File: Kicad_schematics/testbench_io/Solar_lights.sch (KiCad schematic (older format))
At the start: 9 parts

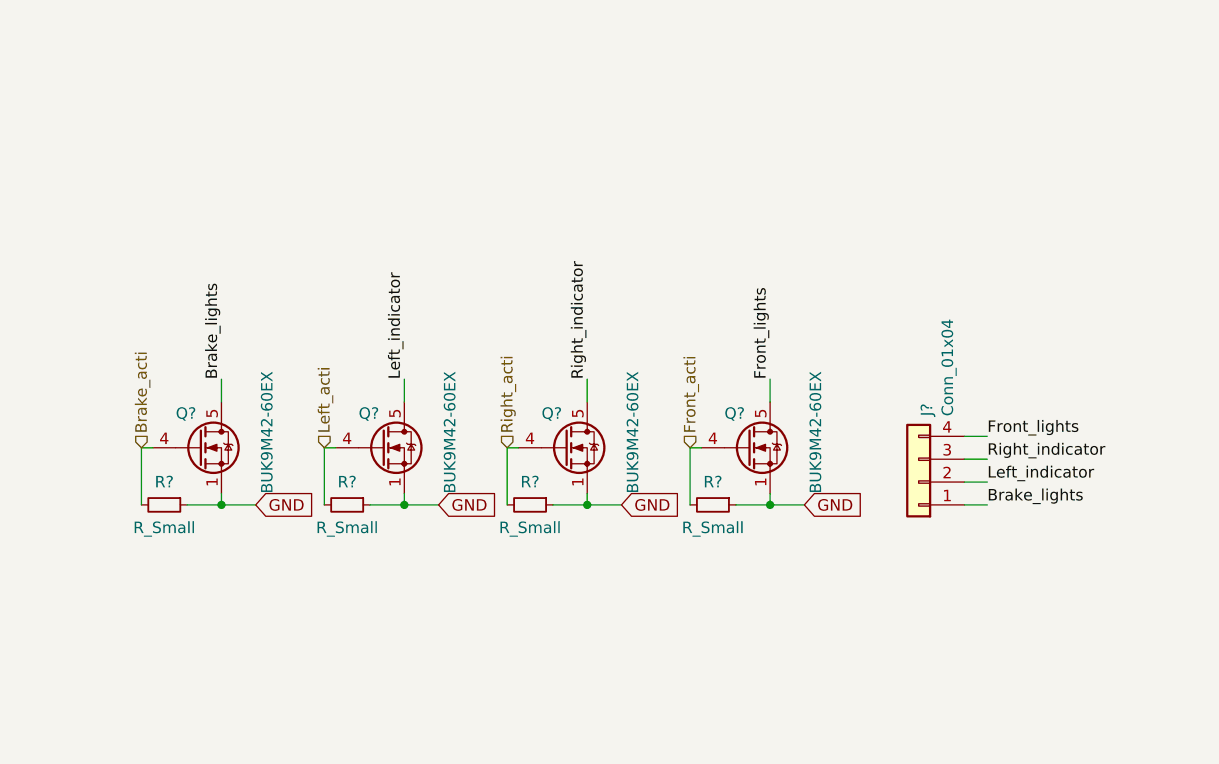
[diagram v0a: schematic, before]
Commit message: Added footprints
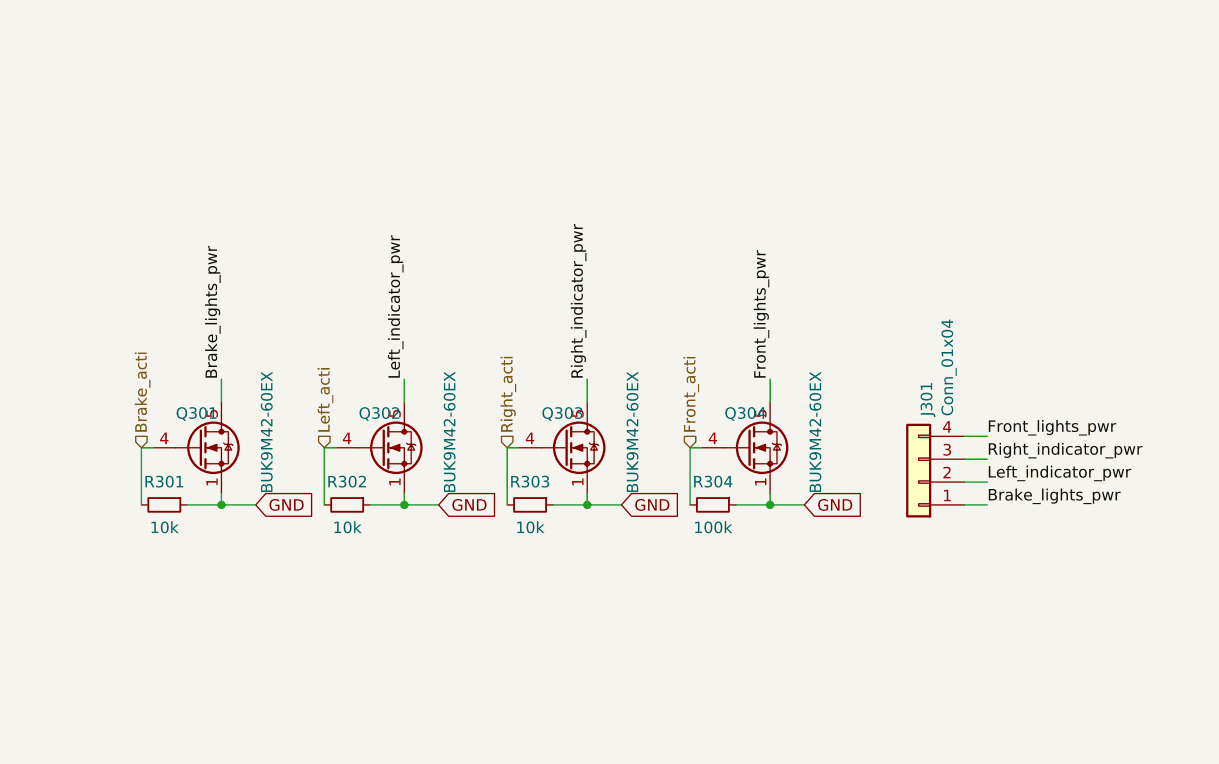
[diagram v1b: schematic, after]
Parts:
- R301, R302, R303: renamed from R?; value R_Small -> 10k
- R304: renamed from R?; value R_Small -> 100k
- gave numbers to parts that had none: 5
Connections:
- net Brake_lights renamed Brake_lights_pwr
- net Front_lights renamed Front_lights_pwr
- net Left_indicator renamed Left_indicator_pwr
- net Right_indicator renamed Right_indicator_pwr
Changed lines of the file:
@@
 	6750 3850 6750 3750
 Text Label 6750 3750 1    50   ~ 0
-Front_lights
+Front_lights_pwr
 Text GLabel 6900 4300 2    50   Input ~ 0
 GND
@@
 P 6500 4300
 AR Path="/60041E0C" Ref="R?"  Part="1"
-AR Path="/6001478F/60041E0C" Ref="R?"  Part="1"
-F 0 "R?" V 6400 4300 50  0000 C CNN
-F 1 "R_Small" V 6600 4300 50  0000 C CNN
+AR Path="/6001478F/60041E0C" Ref="R304"  Part="1"
+F 0 "R304" V 6400 4300 50  0000 C CNN
+F 1 "100k" V 6600 4300 50  0000 C CNN
 F 2 "" H 6500 4300 50  0001 C CNN
 F 3 "~" H 6500 4300 50  0001 C CNN
@@
 P 6650 4050
 AR Path="/60041E12" Ref="Q?"  Part="1"
-AR Path="/6001478F/60041E12" Ref="Q?"  Part="1"
-F 0 "Q?" H 6550 4200 50  0000 L CNN
+AR Path="/6001478F/60041E12" Ref="Q304"  Part="1"
+F 0 "Q304" H 6550 4200 50  0000 L CNN
 F 1 "BUK9M42-60EX" V 6950 3850 50  0000 L CNN
 F 2 "Package_TO_SOT_SMD:LFPAK33" H 6850 3975 50  0001 L CIN
@@
 	5950 3850 5950 3750
 Text Label 5950 3750 1    50   ~ 0
-Right_indicator
+Right_indicator_pwr
 Text GLabel 6100 4300 2    50   Input ~ 0
 GND
@@
 P 5700 4300
 AR Path="/60041E22" Ref="R?"  Part="1"
-AR Path="/6001478F/60041E22" Ref="R?"  Part="1"
-F 0 "R?" V 5600 4300 50  0000 C CNN
-F 1 "R_Small" V 5800 4300 50  0000 C CNN
+AR Path="/6001478F/60041E22" Ref="R303"  Part="1"
+F 0 "R303" V 5600 4300 50  0000 C CNN
+F 1 "10k" V 5800 4300 50  0000 C CNN
 F 2 "" H 5700 4300 50  0001 C CNN
 F 3 "~" H 5700 4300 50  0001 C CNN
@@
 P 5850 4050
 AR Path="/60041E28" Ref="Q?"  Part="1"
-AR Path="/6001478F/60041E28" Ref="Q?"  Part="1"
-F 0 "Q?" H 5750 4200 50  0000 L CNN
+AR Path="/6001478F/60041E28" Ref="Q303"  Part="1"
+F 0 "Q303" H 5750 4200 50  0000 L CNN
 F 1 "BUK9M42-60EX" V 6150 3850 50  0000 L CNN
 F 2 "Package_TO_SOT_SMD:LFPAK33" H 6050 3975 50  0001 L CIN
@@
 	5150 3850 5150 3750
 Text Label 5150 3750 1    50   ~ 0
-Left_indicator
+Left_indicator_pwr
 Text GLabel 5300 4300 2    50   Input ~ 0
 GND
@@
 P 4900 4300
 AR Path="/60041E38" Ref="R?"  Part="1"
-AR Path="/6001478F/60041E38" Ref="R?"  Part="1"
-F 0 "R?" V 4800 4300 50  0000 C CNN
-F 1 "R_Small" V 5000 4300 50  0000 C CNN
+AR Path="/6001478F/60041E38" Ref="R302"  Part="1"
+F 0 "R302" V 4800 4300 50  0000 C CNN
+F 1 "10k" V 5000 4300 50  0000 C CNN
 F 2 "" H 4900 4300 50  0001 C CNN
 F 3 "~" H 4900 4300 50  0001 C CNN
@@
 P 5050 4050
 AR Path="/60041E3E" Ref="Q?"  Part="1"
-AR Path="/6001478F/60041E3E" Ref="Q?"  Part="1"
-F 0 "Q?" H 4950 4200 50  0000 L CNN
+AR Path="/6001478F/60041E3E" Ref="Q302"  Part="1"
+F 0 "Q302" H 4950 4200 50  0000 L CNN
 F 1 "BUK9M42-60EX" V 5350 3850 50  0000 L CNN
 F 2 "Package_TO_SOT_SMD:LFPAK33" H 5250 3975 50  0001 L CIN
@@
 	4350 3850 4350 3750
 Text Label 4350 3750 1    50   ~ 0
-Brake_lights
+Brake_lights_pwr
 Text GLabel 4500 4300 2    50   Input ~ 0
 GND
@@
 P 4100 4300
 AR Path="/60041E4E" Ref="R?"  Part="1"
-AR Path="/6001478F/60041E4E" Ref="R?"  Part="1"
-F 0 "R?" V 4000 4300 50  0000 C CNN
-F 1 "R_Small" V 4200 4300 50  0000 C CNN
+AR Path="/6001478F/60041E4E" Ref="R301"  Part="1"
+F 0 "R301" V 4000 4300 50  0000 C CNN
+F 1 "10k" V 4200 4300 50  0000 C CNN
 F 2 "" H 4100 4300 50  0001 C CNN
 F 3 "~" H 4100 4300 50  0001 C CNN
@@
 P 4250 4050
 AR Path="/60041E54" Ref="Q?"  Part="1"
-AR Path="/6001478F/60041E54" Ref="Q?"  Part="1"
-F 0 "Q?" H 4150 4200 50  0000 L CNN
+AR Path="/6001478F/60041E54" Ref="Q301"  Part="1"
+F 0 "Q301" H 4150 4200 50  0000 L CNN
 F 1 "BUK9M42-60EX" V 4550 3850 50  0000 L CNN
 F 2 "Package_TO_SOT_SMD:LFPAK33" H 4450 3975 50  0001 L CIN
@@
 Front_acti
 $Comp
-L Connector_Generic:Conn_01x04 J?
+L Connector_Generic:Conn_01x04 J301
 U 1 1 60130D83
 P 7400 4200
-F 0 "J?" V 7364 3912 50  0000 R CNN
+F 0 "J301" V 7364 3912 50  0000 R CNN
 F 1 "Conn_01x04" V 7273 3912 50  0000 R CNN
 F 2 "" H 7400 4200 50  0001 C CNN
@@
 $EndComp
 Text Label 7700 4300 0    50   ~ 0
-Brake_lights
+Brake_lights_pwr
 Text Label 7700 4200 0    50   ~ 0
-Left_indicator
+Left_indicator_pwr
 Text Label 7700 4100 0    50   ~ 0
-Right_indicator
+Right_indicator_pwr
 Text Label 7700 4000 0    50   ~ 0
-Front_lights
+Front_lights_pwr
 Wire Wire Line
 	7600 4300 7700 4300

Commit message: Started with layout
Signed-off-by: Mojitas <47667093+Mojitas@users.noreply.github.com>
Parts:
- J301: footprint (none) -> Connector_JST:JST_XH_S4B-XH-A-1_1x04_P2.50mm_Horizontal
- Q301, Q302, Q303, Q304: footprint Package_TO_SOT_SMD:LFPAK33 -> Package_TO_SOT_SMD:TO-252-2
- R301, R302, R303, R304: footprint (none) -> Resistor_SMD:R_0603_1608Metric
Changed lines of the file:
@@
 F 0 "R304" V 6400 4300 50  0000 C CNN
 F 1 "100k" V 6600 4300 50  0000 C CNN
-F 2 "" H 6500 4300 50  0001 C CNN
+F 2 "Resistor_SMD:R_0603_1608Metric" H 6500 4300 50  0001 C CNN
 F 3 "~" H 6500 4300 50  0001 C CNN
 	1    6500 4300
@@
 F 0 "Q304" H 6550 4200 50  0000 L CNN
 F 1 "BUK9M42-60EX" V 6950 3850 50  0000 L CNN
-F 2 "Package_TO_SOT_SMD:LFPAK33" H 6850 3975 50  0001 L CIN
+F 2 "Package_TO_SOT_SMD:TO-252-2" H 6850 3975 50  0001 L CIN
 F 3 "https://assets.nexperia.com/documents/data-sheet/BUK9M42-60E.pdf" V 6650 4050 50  0001 L CNN
 	1    6650 4050
@@
 F 0 "R303" V 5600 4300 50  0000 C CNN
 F 1 "10k" V 5800 4300 50  0000 C CNN
-F 2 "" H 5700 4300 50  0001 C CNN
+F 2 "Resistor_SMD:R_0603_1608Metric" H 5700 4300 50  0001 C CNN
 F 3 "~" H 5700 4300 50  0001 C CNN
 	1    5700 4300
@@
 F 0 "Q303" H 5750 4200 50  0000 L CNN
 F 1 "BUK9M42-60EX" V 6150 3850 50  0000 L CNN
-F 2 "Package_TO_SOT_SMD:LFPAK33" H 6050 3975 50  0001 L CIN
+F 2 "Package_TO_SOT_SMD:TO-252-2" H 6050 3975 50  0001 L CIN
 F 3 "https://assets.nexperia.com/documents/data-sheet/BUK9M42-60E.pdf" V 5850 4050 50  0001 L CNN
 	1    5850 4050
@@
 F 0 "R302" V 4800 4300 50  0000 C CNN
 F 1 "10k" V 5000 4300 50  0000 C CNN
-F 2 "" H 4900 4300 50  0001 C CNN
+F 2 "Resistor_SMD:R_0603_1608Metric" H 4900 4300 50  0001 C CNN
 F 3 "~" H 4900 4300 50  0001 C CNN
 	1    4900 4300
@@
 F 0 "Q302" H 4950 4200 50  0000 L CNN
 F 1 "BUK9M42-60EX" V 5350 3850 50  0000 L CNN
-F 2 "Package_TO_SOT_SMD:LFPAK33" H 5250 3975 50  0001 L CIN
+F 2 "Package_TO_SOT_SMD:TO-252-2" H 5250 3975 50  0001 L CIN
 F 3 "https://assets.nexperia.com/documents/data-sheet/BUK9M42-60E.pdf" V 5050 4050 50  0001 L CNN
 	1    5050 4050
@@
 F 0 "R301" V 4000 4300 50  0000 C CNN
 F 1 "10k" V 4200 4300 50  0000 C CNN
-F 2 "" H 4100 4300 50  0001 C CNN
+F 2 "Resistor_SMD:R_0603_1608Metric" H 4100 4300 50  0001 C CNN
 F 3 "~" H 4100 4300 50  0001 C CNN
 	1    4100 4300
@@
 F 0 "Q301" H 4150 4200 50  0000 L CNN
 F 1 "BUK9M42-60EX" V 4550 3850 50  0000 L CNN
-F 2 "Package_TO_SOT_SMD:LFPAK33" H 4450 3975 50  0001 L CIN
+F 2 "Package_TO_SOT_SMD:TO-252-2" H 4450 3975 50  0001 L CIN
 F 3 "https://assets.nexperia.com/documents/data-sheet/BUK9M42-60E.pdf" V 4250 4050 50  0001 L CNN
 	1    4250 4050
@@
 F 0 "J301" V 7364 3912 50  0000 R CNN
 F 1 "Conn_01x04" V 7273 3912 50  0000 R CNN
-F 2 "" H 7400 4200 50  0001 C CNN
+F 2 "Connector_JST:JST_XH_S4B-XH-A-1_1x04_P2.50mm_Horizontal" H 7400 4200 50  0001 C CNN
 F 3 "~" H 7400 4200 50  0001 C CNN
 	1    7400 4200

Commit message: Pcb-layout is on the way
Signed-off-by: Mojitas <47667093+Mojitas@users.noreply.github.com>
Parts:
- removed Q301, Q302, Q303, Q304: BUK9M42-60EX, Package_TO_SOT_SMD:TO-252-2, symbol Transistor_FET:BUK9M42-60EX
- added Q301, Q302, Q303, Q304: IPD50R380CE, Package_TO_SOT_SMD:TO-252-2, symbol Transistor_FET:IPD50R380CE
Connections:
- net Brake_acti: now also Q301.1 (G)
- net Brake_lights_pwr: now also Q301.2 (D)
- net Front_acti: now also Q304.1 (G)
- net Front_lights_pwr: now also Q304.2 (D)
- net GND: now also Q301.3 (S), Q302.3 (S), Q303.3 (S), Q304.3 (S)
- net Left_acti: now also Q302.1 (G)
- net Left_indicator_pwr: now also Q302.2 (D)
- net Right_acti: now also Q303.1 (G)
- net Right_indicator_pwr: now also Q303.2 (D)
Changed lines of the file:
@@
 	0    1    1    0
-$EndComp
-$Comp
-L Transistor_FET:BUK9M42-60EX Q?
-U 1 1 60041E12
-P 6650 4050
-AR Path="/60041E12" Ref="Q?"  Part="1"
-AR Path="/6001478F/60041E12" Ref="Q304"  Part="1"
-F 0 "Q304" H 6550 4200 50  0000 L CNN
-F 1 "BUK9M42-60EX" V 6950 3850 50  0000 L CNN
-F 2 "Package_TO_SOT_SMD:TO-252-2" H 6850 3975 50  0001 L CIN
-F 3 "https://assets.nexperia.com/documents/data-sheet/BUK9M42-60E.pdf" V 6650 4050 50  0001 L CNN
-	1    6650 4050
-	1    0    0    -1
 $EndComp
 Wire Wire Line
@@
 	0    1    1    0
 $EndComp
-$Comp
-L Transistor_FET:BUK9M42-60EX Q?
-U 1 1 60041E28
-P 5850 4050
-AR Path="/60041E28" Ref="Q?"  Part="1"
-AR Path="/6001478F/60041E28" Ref="Q303"  Part="1"
-F 0 "Q303" H 5750 4200 50  0000 L CNN
-F 1 "BUK9M42-60EX" V 6150 3850 50  0000 L CNN
-F 2 "Package_TO_SOT_SMD:TO-252-2" H 6050 3975 50  0001 L CIN
-F 3 "https://assets.nexperia.com/documents/data-sheet/BUK9M42-60E.pdf" V 5850 4050 50  0001 L CNN
-	1    5850 4050
-	1    0    0    -1
-$EndComp
 Wire Wire Line
 	5150 3850 5150 3750
@@
 	0    1    1    0
 $EndComp
-$Comp
-L Transistor_FET:BUK9M42-60EX Q?
-U 1 1 60041E3E
-P 5050 4050
-AR Path="/60041E3E" Ref="Q?"  Part="1"
-AR Path="/6001478F/60041E3E" Ref="Q302"  Part="1"
-F 0 "Q302" H 4950 4200 50  0000 L CNN
-F 1 "BUK9M42-60EX" V 5350 3850 50  0000 L CNN
-F 2 "Package_TO_SOT_SMD:TO-252-2" H 5250 3975 50  0001 L CIN
-F 3 "https://assets.nexperia.com/documents/data-sheet/BUK9M42-60E.pdf" V 5050 4050 50  0001 L CNN
-	1    5050 4050
-	1    0    0    -1
-$EndComp
 Wire Wire Line
 	4350 3850 4350 3750
@@
 	1    4100 4300
 	0    1    1    0
-$EndComp
-$Comp
-L Transistor_FET:BUK9M42-60EX Q?
-U 1 1 60041E54
-P 4250 4050
-AR Path="/60041E54" Ref="Q?"  Part="1"
-AR Path="/6001478F/60041E54" Ref="Q301"  Part="1"
-F 0 "Q301" H 4150 4200 50  0000 L CNN
-F 1 "BUK9M42-60EX" V 4550 3850 50  0000 L CNN
-F 2 "Package_TO_SOT_SMD:TO-252-2" H 4450 3975 50  0001 L CIN
-F 3 "https://assets.nexperia.com/documents/data-sheet/BUK9M42-60E.pdf" V 4250 4050 50  0001 L CNN
-	1    4250 4050
-	1    0    0    -1
 $EndComp
 Text HLabel 4000 4050 1    50   Input ~ 0
@@
 Wire Wire Line
 	7600 4200 7700 4200
+$Comp
+L Transistor_FET:IPD50R380CE Q301
+U 1 1 600FBD09
+P 4250 4050
+F 0 "Q301" H 4455 4096 50  0000 L CNN
+F 1 "IPD50R380CE" H 4455 4005 50  0000 L CNN
+F 2 "Package_TO_SOT_SMD:TO-252-2" H 4450 3975 50  0001 L CIN
+F 3 "https://www.infineon.com/dgdl/Infineon-IPD50R380CE-DS-v02_01-en.pdf?fileId=db3a30433ecb86d4013ed0a2ef580f38" H 4250 4050 50  0001 L CNN
+	1    4250 4050
+	1    0    0    -1
+$EndComp
+$Comp
+L Transistor_FET:IPD50R380CE Q302
+U 1 1 600FF05E
+P 5050 4050
+F 0 "Q302" H 5255 4096 50  0000 L CNN
+F 1 "IPD50R380CE" H 5255 4005 50  0000 L CNN
+F 2 "Package_TO_SOT_SMD:TO-252-2" H 5250 3975 50  0001 L CIN
+F 3 "https://www.infineon.com/dgdl/Infineon-IPD50R380CE-DS-v02_01-en.pdf?fileId=db3a30433ecb86d4013ed0a2ef580f38" H 5050 4050 50  0001 L CNN
+	1    5050 4050
+	1    0    0    -1
+$EndComp
+$Comp
+L Transistor_FET:IPD50R380CE Q303
+U 1 1 600FF654
+P 5850 4050
+F 0 "Q303" H 6055 4096 50  0000 L CNN
+F 1 "IPD50R380CE" H 6055 4005 50  0000 L CNN
+F 2 "Package_TO_SOT_SMD:TO-252-2" H 6050 3975 50  0001 L CIN
+F 3 "https://www.infineon.com/dgdl/Infineon-IPD50R380CE-DS-v02_01-en.pdf?fileId=db3a30433ecb86d4013ed0a2ef580f38" H 5850 4050 50  0001 L CNN
+	1    5850 4050
+	1    0    0    -1
+$EndComp
+$Comp
+L Transistor_FET:IPD50R380CE Q304
+U 1 1 600FFC56
+P 6650 4050
+F 0 "Q304" H 6855 4096 50  0000 L CNN
+F 1 "IPD50R380CE" H 6855 4005 50  0000 L CNN
+F 2 "Package_TO_SOT_SMD:TO-252-2" H 6850 3975 50  0001 L CIN
+F 3 "https://www.infineon.com/dgdl/Infineon-IPD50R380CE-DS-v02_01-en.pdf?fileId=db3a30433ecb86d4013ed0a2ef580f38" H 6650 4050 50  0001 L CNN
+	1    6650 4050
+	1    0    0    -1
+$EndComp
 $EndSCHEMATC

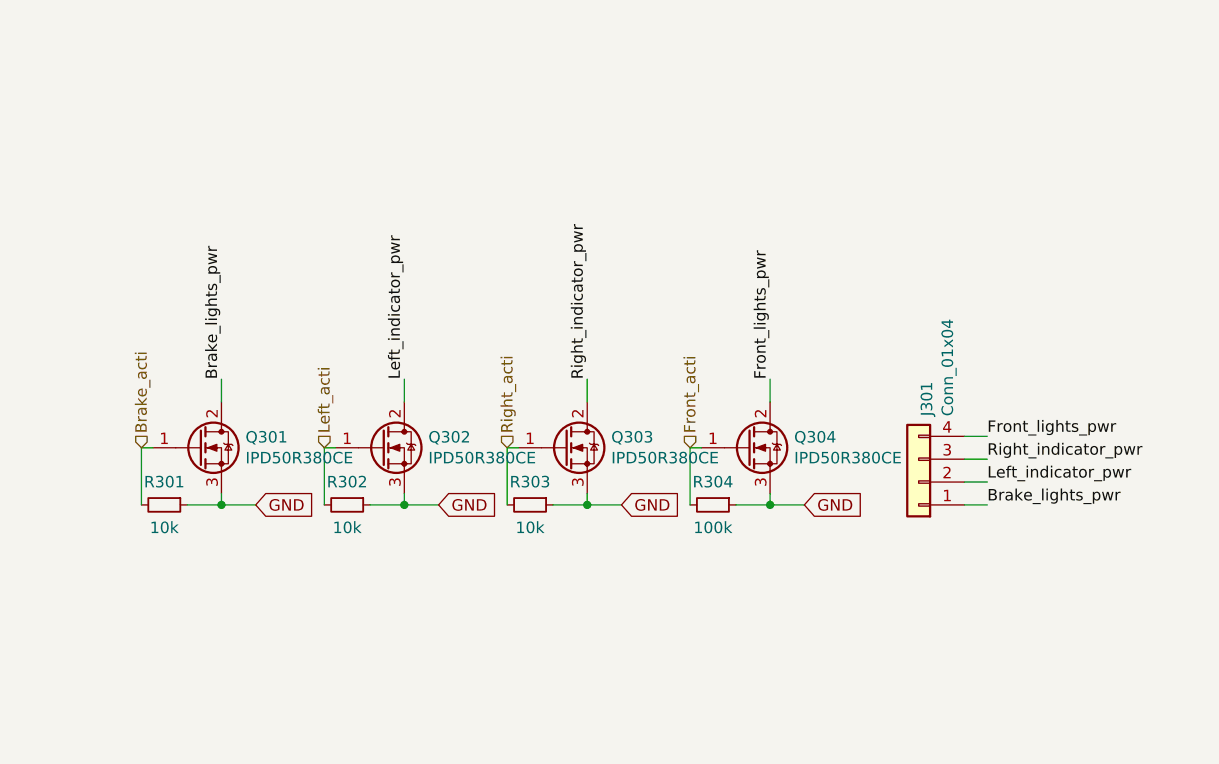
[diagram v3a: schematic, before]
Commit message: Routing done and power planes added
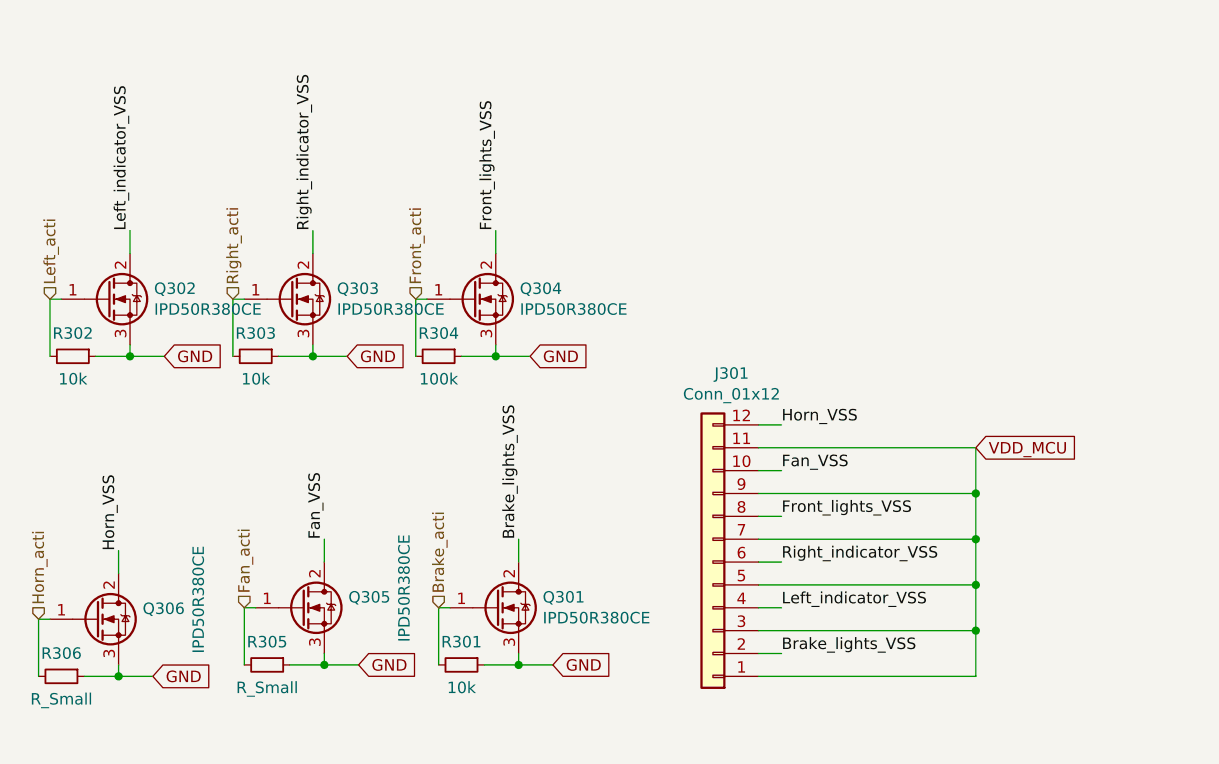
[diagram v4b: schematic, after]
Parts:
- removed J301: Conn_01x04, Connector_JST:JST_XH_S4B-XH-A-1_1x04_P2.50mm_Horizontal, symbol Connector_Generic:Conn_01x04
- added J301: Conn_01x12, Connector_JST:JST_XH_S12B-XH-A-1_1x12_P2.50mm_Horizontal, symbol Connector_Generic:Conn_01x12
- added Q305, Q306: IPD50R380CE, Package_TO_SOT_SMD:TO-252-2, symbol Transistor_FET:IPD50R380CE
- added R305, R306: R_Small, Resistor_SMD:R_0603_1608Metric, symbol Device:R_Small
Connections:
- net GND: now also Q305.3 (S), Q306.3 (S), R305.1, R306.1
- net Brake_lights_pwr renamed Brake_lights_VSS
- net Brake_lights_VSS: now also J301.2 (Pin_2)
- net Front_lights_pwr renamed Front_lights_VSS
- net Front_lights_VSS: now also J301.8 (Pin_8)
- net Left_indicator_pwr renamed Left_indicator_VSS
- net Left_indicator_VSS: now also J301.4 (Pin_4)
- net Right_indicator_pwr renamed Right_indicator_VSS
- net Right_indicator_VSS: now also J301.6 (Pin_6)
- new net Fan_VSS: J301.10 (Pin_10), Q305.2 (D)
- new net Fan_acti: Q305.1 (G), R305.2
- new net Horn_VSS: J301.12 (Pin_12), Q306.2 (D)
- new net Horn_acti: Q306.1 (G), R306.2
- new net VDD_MCU: J301.1 (Pin_1), J301.11 (Pin_11), J301.3 (Pin_3), J301.5 (Pin_5), J301.7 (Pin_7), J301.9 (Pin_9)
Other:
- moved on the sheet: Q301, Q302, Q303, Q304, R301, R302, R303, R304
